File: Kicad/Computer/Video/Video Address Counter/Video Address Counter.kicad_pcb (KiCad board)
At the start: 2 copper layers, 18.8 x 73.8 mm, 16 parts, among them IC1 AP7365-33WG-7, IC10 74LVC161PW,112, IC3 74LVC161PW,112, IC4 74LVC161PW,112, IC6 74LVC161PW,112, IC7 74LVC161PW,112, IC9 74LVC161PW,112, J1 Conn_02x32_Counter_Clockwise

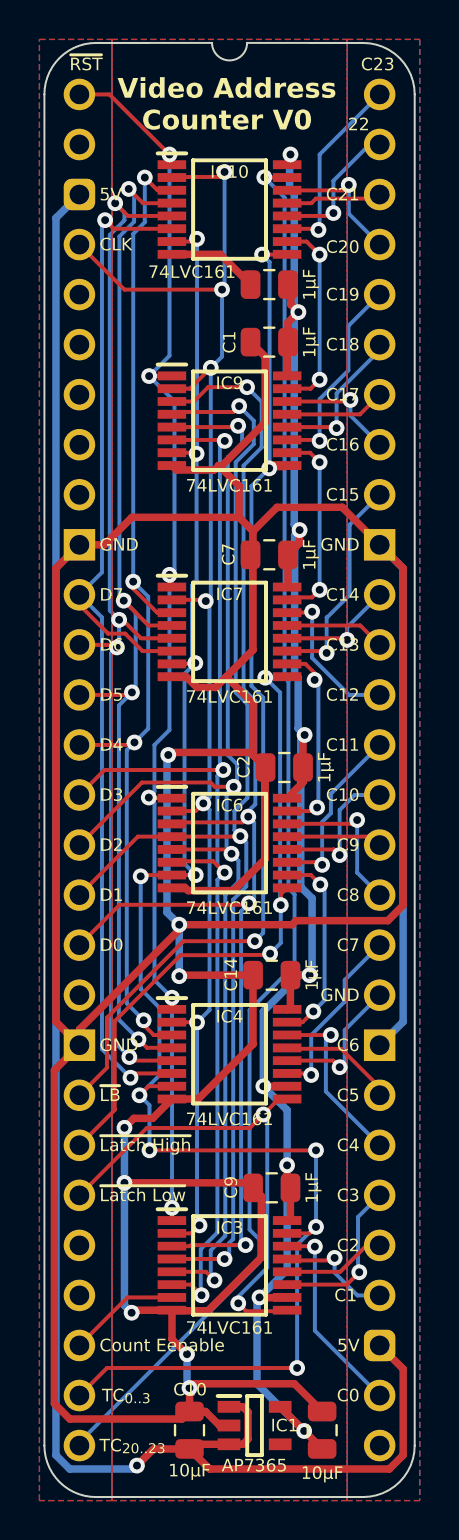
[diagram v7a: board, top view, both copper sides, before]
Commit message: Fixed Video Address Counter.
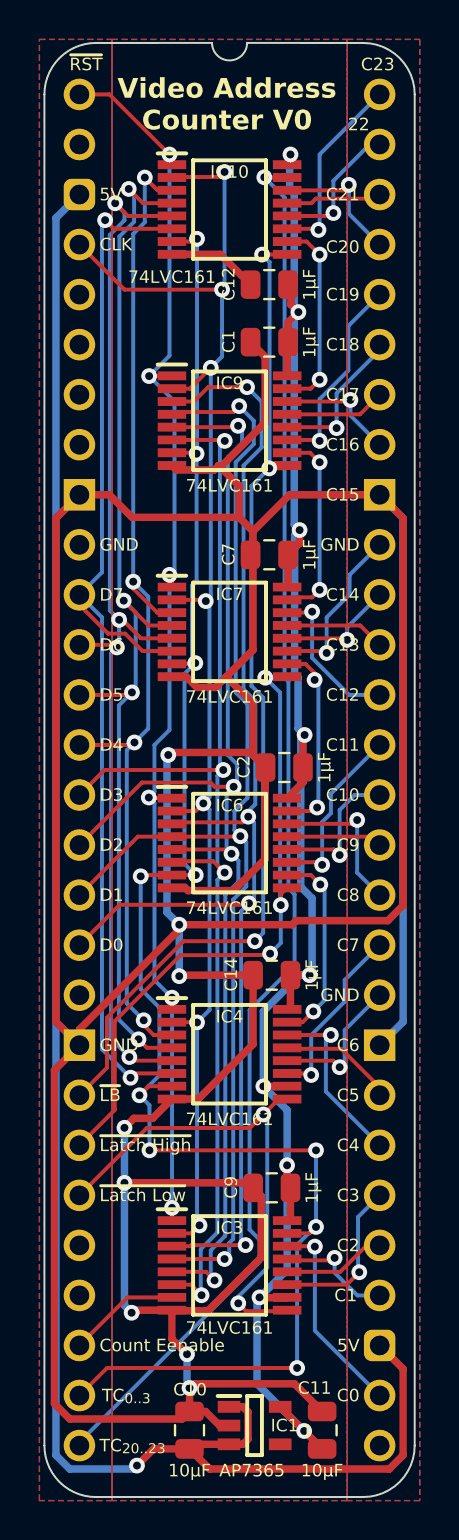
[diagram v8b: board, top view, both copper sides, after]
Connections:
- net /5V renamed 5V
- net /C0 renamed C0
- net /C1 renamed C1
- net /C10 renamed C10
- net /C11 renamed C11
- net /C12 renamed C12
- net /C13 renamed C13
- net /C14 renamed C14
- net /C16 renamed C16
- net /C17 renamed C17
- net /C18 renamed C18
- net /C19 renamed C19
- net /C2 renamed C2
- net /C20 renamed C20
- net /C21 renamed C21
- net /C22 renamed C22
- net /C23 renamed C23
- net /C3 renamed C3
- net /C4 renamed C4
- net /C5 renamed C5
- net /C6 renamed C6
- net /C7 renamed C7
- net /C8 renamed C8
- net /C9 renamed C9
- net /CLK renamed CLK
- net /Count Enable renamed Count Enable
- net /D0 renamed D0
- net /D1 renamed D1
- net /D2 renamed D2
- net /D3 renamed D3
- net /D4 renamed D4
- net /D5 renamed D5
- net /D6 renamed D6
- net /D7 renamed D7
- net /TC_{0..3} renamed TC_{0..3}
- net /TC_{20..23} renamed TC_{20..23}
- net /~{Latch Bank} renamed ~{Latch Bank}
- net /~{Latch High} renamed ~{Latch High}
- net /~{Latch Low} renamed ~{Latch Low}
- net /~{Reset} renamed ~{Reset}
- C1 pad 2: /GND -> GND
- C10 pad 2: /GND -> GND
- C11 pad 2: /GND -> GND
- C12 pad 2: /GND -> GND
- C14 pad 2: /GND -> GND
- C2 pad 2: /GND -> GND
- C7 pad 2: /GND -> GND
- C9 pad 2: /GND -> GND
- IC1 pad 2: /GND -> GND
- IC10 pad 8: /GND -> GND
- IC3 pad 8: /GND -> GND
- IC4 pad 8: /GND -> GND
- IC6 pad 8: /GND -> GND
- IC7 pad 11: /C15 -> C15
- IC7 pad 8: /GND -> GND
- IC9 pad 8: /GND -> GND
- J1 pad 10: /GND -> unconnected-(J1-Pin_10-Pad10)
- J1 pad 20: /GND -> GND
- J1 pad 37: /GND -> GND
- J1 pad 47: /GND -> C15
- J1 pad 48: /C15 -> GND
- J1 pad 9: unconnected-(J1-Pin_9-Pad9) -> GND
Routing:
- net GND: track 0.00 -> 260.5 mm, vias 0 -> 8
- net /GND: track 253.5 -> 0.00 mm, vias 8 -> 0
- net /C15: track 11.2 -> 0.00 mm, vias 1 -> 0
- net C15: track 0.00 -> 8.65 mm, vias 0 -> 1
- added copper zone on B.Cu, net GND
- added copper zone on F.Cu, net GND
- removed copper zone on B.Cu, net /GND
- removed copper zone on F.Cu, net /GND
